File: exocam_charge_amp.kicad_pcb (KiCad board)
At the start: 2 copper layers, 16.5 x 14 mm, 8 parts, among them J1 dupont2x1, U1 TLV2771CDBVT

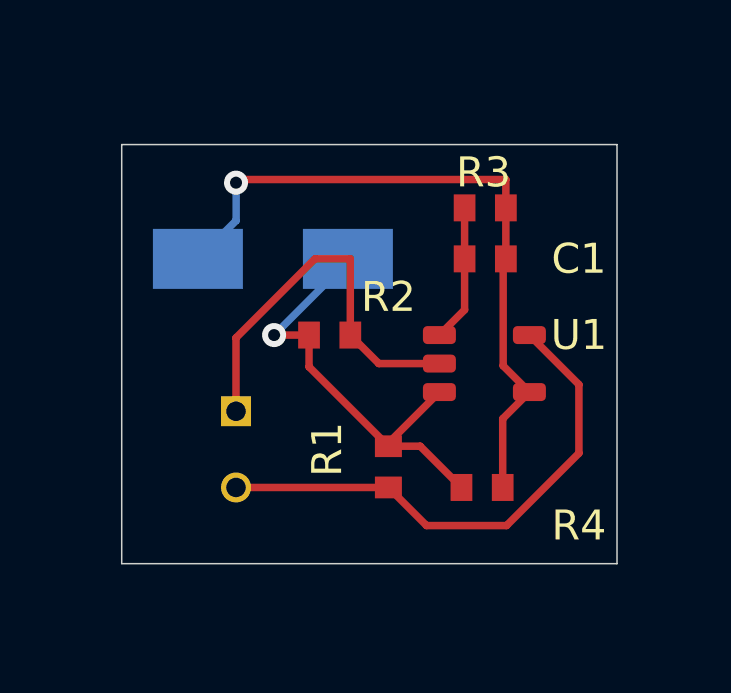
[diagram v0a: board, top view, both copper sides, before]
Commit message: added step and updated to have screw mounts for the board
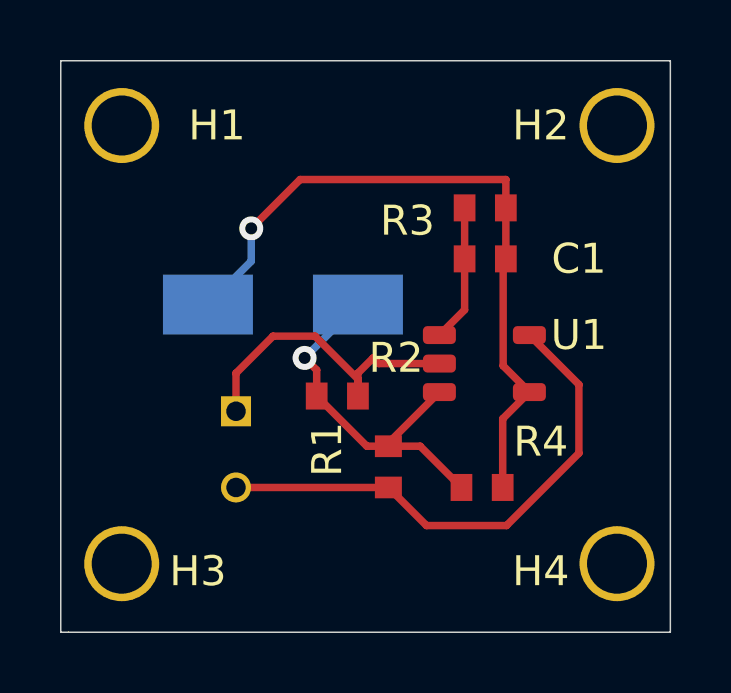
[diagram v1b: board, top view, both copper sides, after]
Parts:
- added H1: MountingHole, exocam_charge_amp:mount_hole_2.5mm, F.Cu at (55.9, 47.6)
- added H2: MountingHole, exocam_charge_amp:mount_hole_2.5mm, F.Cu at (72.4, 47.6)
- added H3: MountingHole, exocam_charge_amp:mount_hole_2.5mm, F.Cu at (55.9, 62.2)
- added H4: MountingHole, exocam_charge_amp:mount_hole_2.5mm, F.Cu at (72.4, 62.2)
- moved R2 2.05 mm to (62.4, 57.9)
- moved BZ1 1.56 mm to (60.0, 59.9)
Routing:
- net Net-(BZ1-Pad2): track 15.0 -> 12.5 mm
- net GND: track 13.3 -> 10.8 mm
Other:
- board size 16.5 x 14 mm -> 20.3 x 19 mm
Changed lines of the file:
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@@
     (thickness 1.6)
     (drawings 5)
-    (tracks 38)
+    (tracks 40)
     (zones 0)
-    (modules 8)
+    (modules 12)
     (nets 6)
   )
@@
       (outputformat 1)
       (mirror false)
-      (drillshape 1)
+      (drillshape 0)
       (scaleselection 1)
-      (outputdirectory ""))
+      (outputdirectory "gerbel_output/"))
   )
   (net 0 "")
@@
     (add_net "Net-(C1-Pad2)")
   )
+  (module exocam_charge_amp:mount_hole_2.5mm (layer F.Cu)
+    (at 72.39 62.23)
+    (fp_text reference H4 (at -3.81 4.064) (layer F.SilkS)
+      (effects (font (size 1 1) (thickness 0.15)))
+    )
+    (fp_text value MountingHole (at 0 -0.5) (layer F.Fab)
+      (effects (font (size 1 1) (thickness 0.15)))
+    )
+    (pad 1 thru_hole circle (at -1.27 3.81) (size 2.5 2.5) (drill 2) (layers *.Cu *.Mask))
+  )
+  (module exocam_charge_amp:mount_hole_2.5mm (layer F.Cu)
+    (at 55.88 62.23)
+    (fp_text reference H3 (at 1.27 4.064) (layer F.SilkS)
+      (effects (font (size 1 1) (thickness 0.15)))
+    )
+    (fp_text value MountingHole (at 0 -0.5) (layer F.Fab)
+      (effects (font (size 1 1) (thickness 0.15)))
+    )
+    (pad 1 thru_hole circle (at -1.27 3.81) (size 2.5 2.5) (drill 2) (layers *.Cu *.Mask))
+  )
+  (module exocam_charge_amp:mount_hole_2.5mm (layer F.Cu)
+    (at 72.39 47.625)
+    (fp_text reference H2 (at -3.81 3.81) (layer F.SilkS)
+      (effects (font (size 1 1) (thickness 0.15)))
+    )
+    (fp_text value MountingHole (at 0 -0.5) (layer F.Fab)
+      (effects (font (size 1 1) (thickness 0.15)))
+    )
+    (pad 1 thru_hole circle (at -1.27 3.81) (size 2.5 2.5) (drill 2) (layers *.Cu *.Mask))
+  )
+  (module exocam_charge_amp:mount_hole_2.5mm (layer F.Cu)
+    (at 55.88 47.625)
+    (fp_text reference H1 (at 1.905 3.81) (layer F.SilkS)
+      (effects (font (size 1 1) (thickness 0.15)))
+    )
+    (fp_text value MountingHole (at 0 -0.5) (layer F.Fab)
+      (effects (font (size 1 1) (thickness 0.15)))
+    )
+    (pad 1 thru_hole circle (at -1.27 3.81) (size 2.5 2.5) (drill 2) (layers *.Cu *.Mask))
+  )
   (module exocam_charge_amp:TLV2271DBV (layer F.Cu)
     (at 66.47 55.88)
@@
   (module exocam_charge_amp:0603_R (layer F.Cu)
     (at 67.205 60.96)
-    (fp_text reference R4 (at 2.645 3.81) (layer F.SilkS)
+    (fp_text reference R4 (at 1.375 1.016) (layer F.SilkS)
       (effects (font (size 1 1) (thickness 0.15)))
     )
@@
   (module exocam_charge_amp:0603_R (layer F.Cu)
     (at 66.145 56.72 180)
-    (fp_text reference R3 (at -0.525 3.72) (layer F.SilkS)
+    (fp_text reference R3 (at 2.01 2.11) (layer F.SilkS)
       (effects (font (size 1 1) (thickness 0.15)))
     )
@@
   )
   (module exocam_charge_amp:0603_R (layer F.Cu)
-    (at 62.125 55.88)
+    (at 62.379 57.912)
     (fp_text reference R2 (at 1.375 1.27) (layer F.SilkS)
       (effects (font (size 1 1) (thickness 0.15)))
@@
       (effects (font (size 1 1) (thickness 0.15)) (justify mirror))
     )
+    (fp_line (start -3.81 -1.27) (end 1.27 -1.27) (layer B.SilkS) (width 0.12))
+    (fp_line (start 1.27 -1.27) (end 1.27 -3.81) (layer B.SilkS) (width 0.12))
+    (fp_line (start 1.27 -3.81) (end -3.81 -3.81) (layer B.SilkS) (width 0.12))
     (fp_line (start -3.81 -3.81) (end -3.81 -1.27) (layer B.SilkS) (width 0.12))
-    (fp_line (start 1.27 -3.81) (end -3.81 -3.81) (layer B.SilkS) (width 0.12))
-    (fp_line (start 1.27 -1.27) (end 1.27 -3.81) (layer B.SilkS) (width 0.12))
-    (fp_line (start -3.81 -1.27) (end 1.27 -1.27) (layer B.SilkS) (width 0.12))
     (pad 2 thru_hole circle (at 0 -2.54 270) (size 1 1) (drill 0.65) (layers *.Cu *.Mask)
       (net 4 +5V))
@@
   )
   (module exocam_charge_amp:piezo_buzzer (layer B.Cu)
-    (at 59.69 58.42)
+    (at 60.024 59.944)
     (fp_text reference BZ1 (at 1.27 -5.08) (layer B.SilkS)
       (effects (font (size 1 1) (thickness 0.15)) (justify mirror))
@@
       (net 2 "Net-(BZ1-Pad1)"))
   )
-  (gr_line (start 54.61 52.07) (end 71.12 52.07) (layer Edge.Cuts) (width 0.05))
-  (gr_line (start 54.61 66.04) (end 71.12 66.04) (layer Edge.Cuts) (width 0.05))
-  (gr_line (start 71.12 66.04) (end 71.12 52.07) (layer Edge.Cuts) (width 0.05))
-  (gr_line (start 54.61 66.04) (end 54.61 52.07) (layer Edge.Cuts) (width 0.05))
-  (gr_circle (center 63.97 57.15) (end 77.47 57.15) (layer Dwgs.User) (width 0.15))
+  (gr_line (start 52.578 68.326) (end 52.578 49.276) (layer Edge.Cuts) (width 0.05))
+  (gr_line (start 52.832 68.326) (end 52.578 68.326) (layer Edge.Cuts) (width 0.05))
+  (gr_line (start 72.898 68.326) (end 52.832 68.326) (layer Edge.Cuts) (width 0.05))
+  (gr_line (start 72.898 49.276) (end 72.898 68.326) (layer Edge.Cuts) (width 0.05))
+  (gr_line (start 52.578 49.276) (end 72.898 49.276) (layer Edge.Cuts) (width 0.05))
   (segment (start 63.5 62.02) (end 65.2 60.32) (width 0.25) (layer F.Cu) (net 1))
   (segment (start 63.5 62.125) (end 63.5 62.02) (width 0.25) (layer F.Cu) (net 1))
   (segment (start 64.56 62.125) (end 65.935 63.5) (width 0.25) (layer F.Cu) (net 1))
   (segment (start 63.5 62.125) (end 64.56 62.125) (width 0.25) (layer F.Cu) (net 1))
-  (segment (start 60.855 59.48) (end 63.5 62.125) (width 0.25) (layer F.Cu) (net 1))
-  (segment (start 60.855 58.42) (end 60.855 58.42) (width 0.25) (layer F.Cu) (net 1))
-  (segment (start 60.855 58.42) (end 60.855 59.48) (width 0.25) (layer F.Cu) (net 1))
-  (via (at 59.69 58.42) (size 0.8) (drill 0.4) (layers F.Cu B.Cu) (net 1))
-  (segment (start 60.855 58.42) (end 59.69 58.42) (width 0.25) (layer F.Cu) (net 1))
-  (segment (start 62.15 55.96) (end 62.15 55.88) (width 0.25) (layer B.Cu) (net 1))
-  (segment (start 59.69 58.42) (end 62.15 55.96) (width 0.25) (layer B.Cu) (net 1))
-  (via (at 58.42 53.34) (size 0.8) (drill 0.4) (layers F.Cu B.Cu) (net 2))
+  (via (at 60.706 59.182) (size 0.8) (drill 0.4) (layers F.Cu B.Cu) (net 1))
+  (segment (start 62.782 62.125) (end 63.5 62.125) (width 0.25) (layer F.Cu) (net 1))
+  (segment (start 61.109 60.452) (end 62.782 62.125) (width 0.25) (layer F.Cu) (net 1))
+  (segment (start 60.706 59.182) (end 62.484 57.404) (width 0.25) (layer B.Cu) (net 1))
+  (segment (start 61.109 59.585) (end 60.706 59.182) (width 0.25) (layer F.Cu) (net 1))
+  (segment (start 61.109 60.452) (end 61.109 59.585) (width 0.25) (layer F.Cu) (net 1))
+  (via (at 58.928 54.864) (size 0.8) (drill 0.4) (layers F.Cu B.Cu) (net 2))
   (segment (start 67.31 61.21) (end 68.2 60.32) (width 0.25) (layer F.Cu) (net 2))
   (segment (start 67.31 63.5) (end 67.31 61.21) (width 0.25) (layer F.Cu) (net 2))
@@
   (segment (start 67.415 55.88) (end 67.32499 55.97001) (width 0.25) (layer F.Cu) (net 2))
   (segment (start 67.415 54.18) (end 67.415 55.88) (width 0.25) (layer F.Cu) (net 2))
+  (segment (start 60.557 53.235) (end 58.928 54.864) (width 0.25) (layer F.Cu) (net 2))
+  (segment (start 67.415 53.235) (end 60.557 53.235) (width 0.25) (layer F.Cu) (net 2))
   (segment (start 67.415 54.18) (end 67.415 53.235) (width 0.25) (layer F.Cu) (net 2))
-  (segment (start 58.525 53.235) (end 58.42 53.34) (width 0.25) (layer F.Cu) (net 2))
-  (segment (start 67.415 53.235) (end 58.525 53.235) (width 0.25) (layer F.Cu) (net 2))
-  (segment (start 58.42 54.61) (end 57.15 55.88) (width 0.25) (layer B.Cu) (net 2))
-  (segment (start 58.42 53.34) (end 58.42 54.61) (width 0.25) (layer B.Cu) (net 2))
+  (segment (start 58.928 55.96) (end 57.484 57.404) (width 0.25) (layer B.Cu) (net 2))
+  (segment (start 58.928 54.864) (end 58.928 55.96) (width 0.25) (layer B.Cu) (net 2))
   (segment (start 66.04 57.58) (end 65.2 58.42) (width 0.25) (layer F.Cu) (net 3))
   (segment (start 66.04 55.88) (end 66.04 57.58) (width 0.25) (layer F.Cu) (net 3))
@@
   (segment (start 69.85 62.357502) (end 69.85 60.07) (width 0.25) (layer F.Cu) (net 4))
   (segment (start 63.18 59.37) (end 65.2 59.37) (width 0.25) (layer F.Cu) (net 5))
-  (segment (start 62.23 58.42) (end 63.18 59.37) (width 0.25) (layer F.Cu) (net 5))
-  (segment (start 62.23 55.88) (end 62.23 58.42) (width 0.25) (layer F.Cu) (net 5))
-  (segment (start 61.051998 55.88) (end 62.23 55.88) (width 0.25) (layer F.Cu) (net 5))
-  (segment (start 58.42 58.511998) (end 61.051998 55.88) (width 0.25) (layer F.Cu) (net 5))
-  (segment (start 58.42 60.96) (end 58.42 58.511998) (width 0.25) (layer F.Cu) (net 5))
+  (segment (start 62.484 59.69) (end 62.992 59.182) (width 0.25) (layer F.Cu) (net 5))
+  (segment (start 62.484 60.452) (end 62.484 59.69) (width 0.25) (layer F.Cu) (net 5))
+  (segment (start 62.992 59.182) (end 63.18 59.37) (width 0.25) (layer F.Cu) (net 5))
+  (segment (start 58.42 60.96) (end 58.42 59.69) (width 0.25) (layer F.Cu) (net 5))
+  (segment (start 62.484 59.886998) (end 62.484 60.452) (width 0.25) (layer F.Cu) (net 5))
+  (segment (start 61.054001 58.456999) (end 62.484 59.886998) (width 0.25) (layer F.Cu) (net 5))
+  (segment (start 59.653001 58.456999) (end 61.054001 58.456999) (width 0.25) (layer F.Cu) (net 5))
+  (segment (start 58.42 59.69) (end 59.653001 58.456999) (width 0.25) (layer F.Cu) (net 5))
 )

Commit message: added output terminals
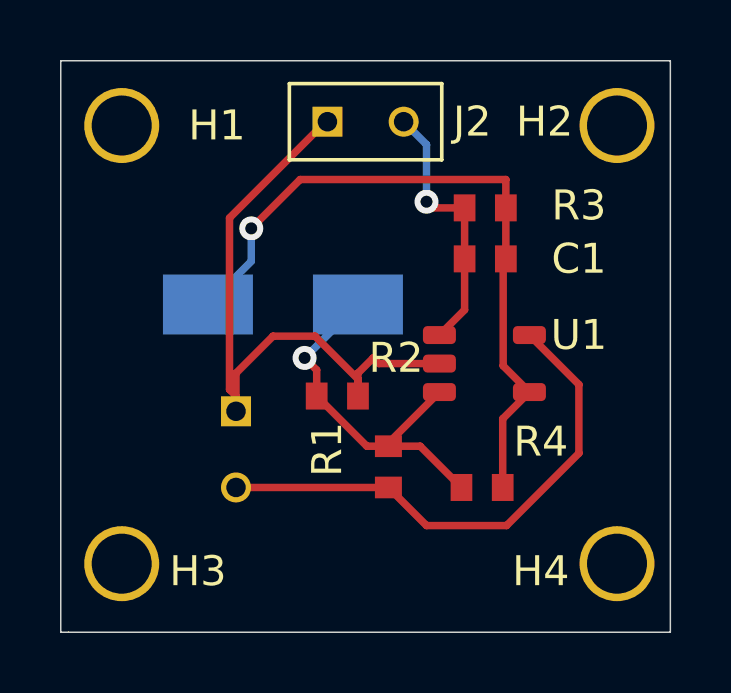
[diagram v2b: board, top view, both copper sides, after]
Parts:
- added J2: dupont2x1, exocam_charge_amp:dupont2x1, F.Cu at (64.0, 48.8)
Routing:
- net GND: track 10.8 -> 21.4 mm
- net Net-(C1-Pad2): track 4.59 -> 8.93 mm, vias 0 -> 1
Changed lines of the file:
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@@
     (thickness 1.6)
     (drawings 5)
-    (tracks 40)
+    (tracks 51)
     (zones 0)
-    (modules 12)
+    (modules 13)
     (nets 6)
   )
@@
     (add_net "Net-(C1-Pad2)")
   )
+  (module exocam_charge_amp:dupont2x1 (layer F.Cu)
+    (at 64.008 48.768)
+    (fp_text reference J2 (at 2.286 2.54) (layer F.SilkS)
+      (effects (font (size 1 1) (thickness 0.15)))
+    )
+    (fp_text value dupont2x1 (at 0 -0.5) (layer F.Fab)
+      (effects (font (size 1 1) (thickness 0.15)))
+    )
+    (fp_line (start -3.81 1.27) (end 1.27 1.27) (layer F.SilkS) (width 0.12))
+    (fp_line (start 1.27 1.27) (end 1.27 3.81) (layer F.SilkS) (width 0.12))
+    (fp_line (start 1.27 3.81) (end -3.81 3.81) (layer F.SilkS) (width 0.12))
+    (fp_line (start -3.81 3.81) (end -3.81 1.27) (layer F.SilkS) (width 0.12))
+    (pad 2 thru_hole circle (at 0 2.54) (size 1 1) (drill 0.65) (layers *.Cu *.Mask)
+      (net 3 "Net-(C1-Pad2)"))
+    (pad 1 thru_hole rect (at -2.54 2.54) (size 1 1) (drill 0.65) (layers *.Cu *.Mask)
+      (net 5 GND))
+  )
   (module exocam_charge_amp:mount_hole_2.5mm (layer F.Cu)
     (at 72.39 62.23)
@@
   (module exocam_charge_amp:mount_hole_2.5mm (layer F.Cu)
     (at 72.39 47.625)
-    (fp_text reference H2 (at -3.81 3.81) (layer F.SilkS)
+    (fp_text reference H2 (at -3.683 3.683) (layer F.SilkS)
       (effects (font (size 1 1) (thickness 0.15)))
     )
@@
   (module exocam_charge_amp:0603_R (layer F.Cu)
     (at 66.145 56.72 180)
-    (fp_text reference R3 (at 2.01 2.11) (layer F.SilkS)
+    (fp_text reference R3 (at -3.705 2.618) (layer F.SilkS)
       (effects (font (size 1 1) (thickness 0.15)))
     )
@@
   (segment (start 66.04 57.58) (end 65.2 58.42) (width 0.25) (layer F.Cu) (net 3))
   (segment (start 66.04 55.88) (end 66.04 57.58) (width 0.25) (layer F.Cu) (net 3))
+  (segment (start 66.04 54.18) (end 66.04 54.18) (width 0.25) (layer F.Cu) (net 3))
   (segment (start 66.04 54.18) (end 66.04 55.88) (width 0.25) (layer F.Cu) (net 3))
+  (via (at 64.77 53.975) (size 0.8) (drill 0.4) (layers F.Cu B.Cu) (net 3))
+  (segment (start 64.975 54.18) (end 64.77 53.975) (width 0.25) (layer F.Cu) (net 3))
+  (segment (start 66.04 54.18) (end 64.975 54.18) (width 0.25) (layer F.Cu) (net 3))
+  (segment (start 64.77 52.07) (end 64.008 51.308) (width 0.25) (layer B.Cu) (net 3))
+  (segment (start 64.77 53.975) (end 64.77 52.07) (width 0.25) (layer B.Cu) (net 3))
   (segment (start 58.42 63.5) (end 63.5 63.5) (width 0.25) (layer F.Cu) (net 4))
   (segment (start 63.5 63.5) (end 64.77 64.77) (width 0.25) (layer F.Cu) (net 4))
@@
   (segment (start 62.484 60.452) (end 62.484 59.69) (width 0.25) (layer F.Cu) (net 5))
   (segment (start 62.992 59.182) (end 63.18 59.37) (width 0.25) (layer F.Cu) (net 5))
-  (segment (start 58.42 60.96) (end 58.42 59.69) (width 0.25) (layer F.Cu) (net 5))
   (segment (start 62.484 59.886998) (end 62.484 60.452) (width 0.25) (layer F.Cu) (net 5))
   (segment (start 61.054001 58.456999) (end 62.484 59.886998) (width 0.25) (layer F.Cu) (net 5))
   (segment (start 59.653001 58.456999) (end 61.054001 58.456999) (width 0.25) (layer F.Cu) (net 5))
   (segment (start 58.42 59.69) (end 59.653001 58.456999) (width 0.25) (layer F.Cu) (net 5))
+  (segment (start 61.410998 51.308) (end 61.468 51.308) (width 0.25) (layer F.Cu) (net 5))
+  (segment (start 58.202999 54.515999) (end 61.410998 51.308) (width 0.25) (layer F.Cu) (net 5))
+  (segment (start 58.202999 60.234999) (end 58.202999 54.515999) (width 0.25) (layer F.Cu) (net 5))
+  (segment (start 58.42 60.96) (end 58.42 60.452) (width 0.25) (layer F.Cu) (net 5))
+  (segment (start 58.42 60.452) (end 58.202999 60.234999) (width 0.25) (layer F.Cu) (net 5))
+  (segment (start 58.42 60.452) (end 58.42 59.69) (width 0.25) (layer F.Cu) (net 5))
 )
